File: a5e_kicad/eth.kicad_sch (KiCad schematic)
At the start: 30 parts, among them J9 RJ45_RB1-125B8G1A, U10 KSZ9031RNXCA

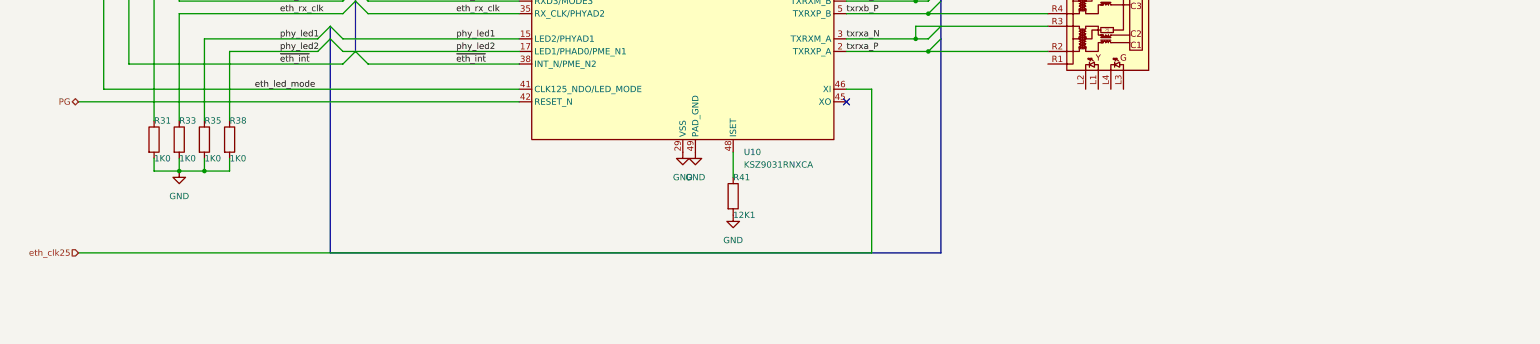
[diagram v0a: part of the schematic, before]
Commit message: fix clock routing and move all components inside board perimeters
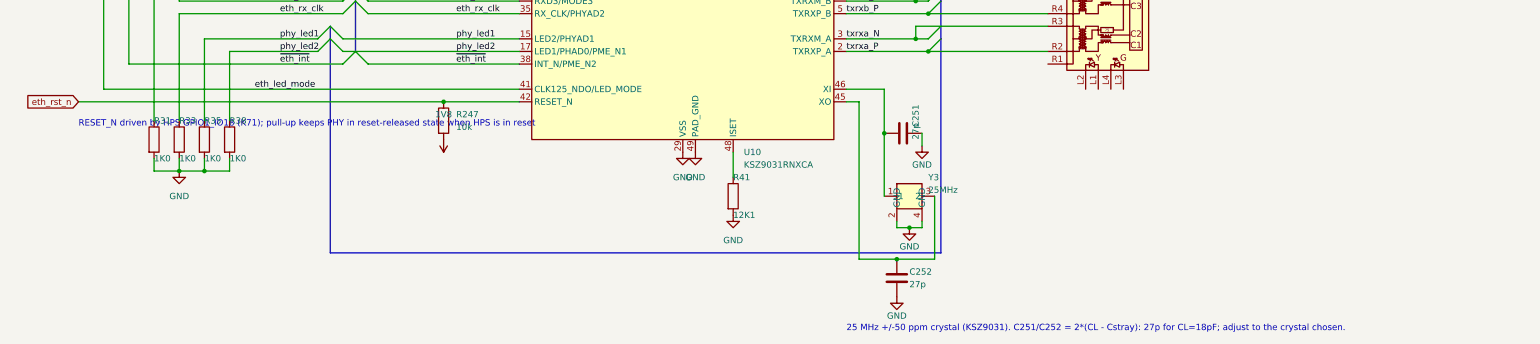
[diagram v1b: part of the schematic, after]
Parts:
- added C251, C252: 27p, Capacitor_SMD:C_0402_1005Metric, symbol Device:C
- added R247: 10k, Resistor_SMD:R_0402_1005Metric, symbol Device:R
- added Y3: 25MHz, Crystal:Crystal_SMD_3225-4Pin_3.2x2.5mm, symbol agilex_5_lib:Crystal_3225
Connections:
- net 1V8: now also R247.2
- net GND: now also C251.2, C252.2, Y3.2 (GND), Y3.4 (GND)
- net at U10.45 (XO): now also C252.1, Y3.3 (2)
- net PG renamed eth_rst_n
- net eth_rst_n: now also R247.1
- net eth_clk25: no longer names the net of U10.46 (XI)
- net eth_clk25: now also C251.1, Y3.1
- no-connect marks 2 -> 1
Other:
- note added: "25 MHz +/-50 ppm crystal (KSZ9031). C251/C252 = 2*(CL - Cstray): 27p for CL=18pF; adjust to the crystal chosen."
- note added: "RESET_N driven by HPS GPIO1_IO18 (K71); pull-up keeps PHY in reset-released state when HPS is in reset"

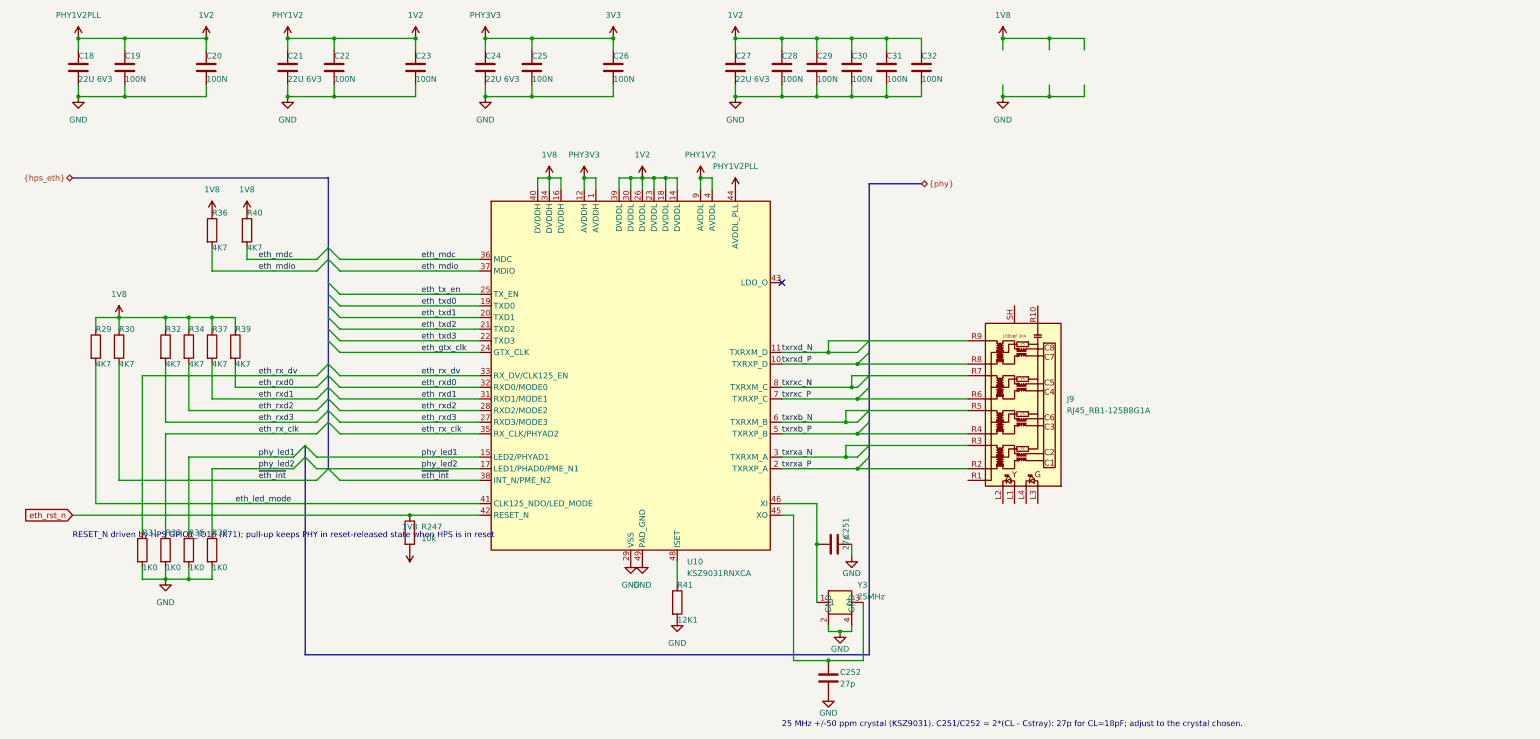
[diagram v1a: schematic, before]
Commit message: fix ethernet jack
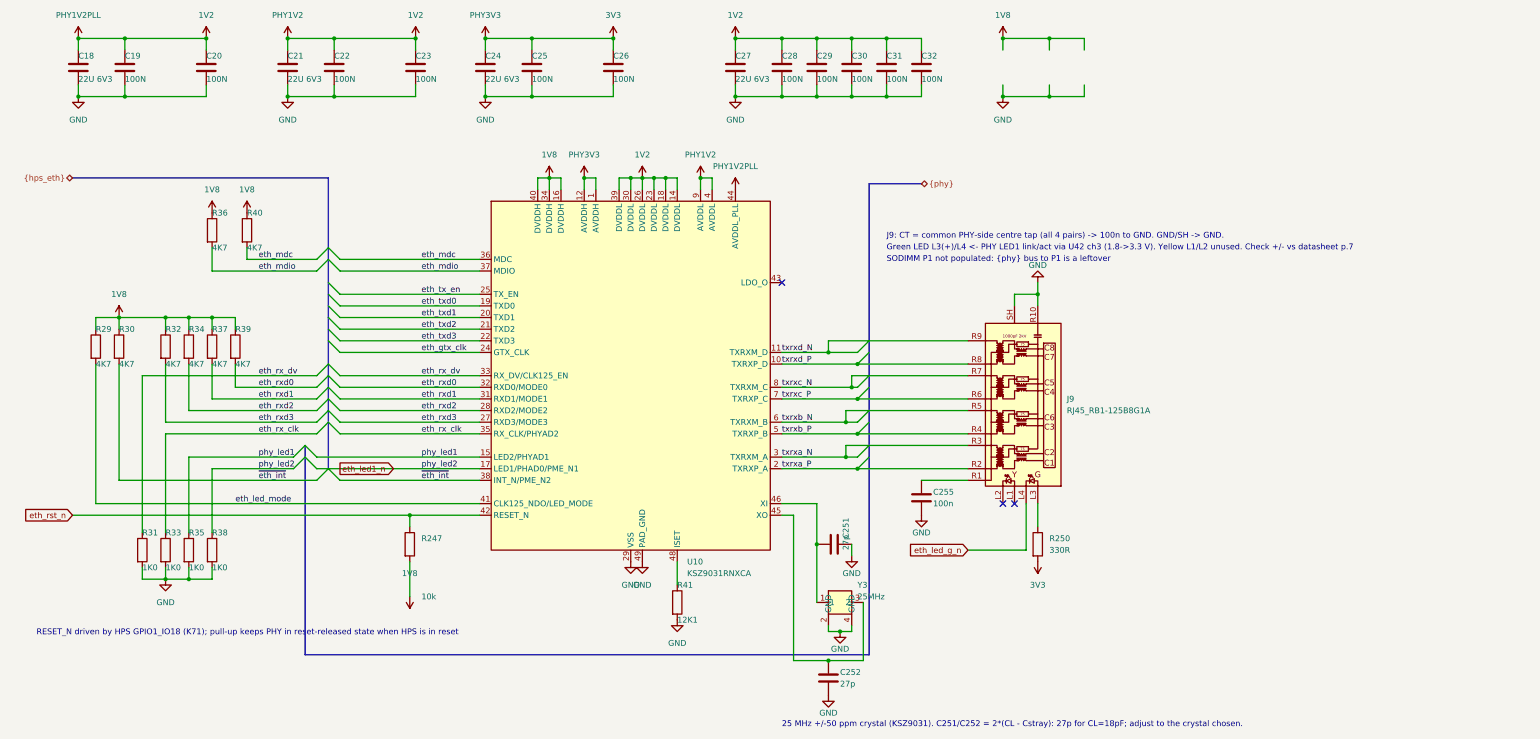
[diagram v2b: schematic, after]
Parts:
- added C255: 100n, Capacitor_SMD:C_0402_1005Metric, symbol Device:C
- added R250: 330R, Resistor_SMD:R_0402_1005Metric, symbol Device:R
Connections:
- net 3V3: now also R250.2
- net GND: now also J9.R10 (GND), J9.SH, C255.2
- net at J9.L3: now also R250.1
- net eth_led_g_n: now reaches J9.L4
- net at J9.R1 (CT): now also C255.1
- net phy_led2 renamed eth_led1_n
- no-connect marks 1 -> 3
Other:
- note added: "Green LED L3(+)/L4 <- PHY LED1 link/act via U42 ch3 (1.8->3.3 V). Yellow L1/L2 unused. Check +/- vs datasheet p.7"
- note added: "J9: CT = common PHY-side centre tap (all 4 pairs) -> 100n to GND. GND/SH -> GND."
- note added: "SODIMM P1 not populated: {phy} bus to P1 is a leftover"
- moved on the sheet: R247
